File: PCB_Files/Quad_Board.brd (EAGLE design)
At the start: 81 x 76.2 mm, 39 parts

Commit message: Updates in layout
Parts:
- moved NAZE32_PINHEAD 6.35 mm to (54.6, 68.6)
- moved ULTRA1 6.35 mm to (12.7, 68.6)
- moved ULTRA4 6.35 mm to (30.5, 68.6)
- moved 5V_PDB 6.35 mm to (8.89, 26.7)
- moved BATTERY_MONITORING_PINS 6.35 mm to (73.7, 48.3)
- moved C1 6.35 mm to (58.4, 36.8)
- moved C10 6.35 mm to (30.5, 38.1)
- moved C15 6.35 mm to (57.1, 24.1)
- moved C2 6.35 mm to (52.1, 36.8)
- moved C3 6.35 mm to (29.2, 29.2)
- moved C4 6.35 mm to (24.1, 29.2)
- moved C7 6.35 mm to (22.9, 38.1)
- moved C9 6.35 mm to (35.6, 41.9)
- moved L1 6.35 mm to (40.6, 34.3)
- moved L2 6.35 mm to (50.8, 24.1)
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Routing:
- net P10.3: track 24.4 -> 48.1 mm, vias 2 -> 3
- net P9.3_5V: track 76.5 -> 74.5 mm, vias 2 -> 1
- net P9.3: track 66.6 -> 68.5 mm
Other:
- board text added: "rev 1.2"
- board text removed: "rev 1.0"

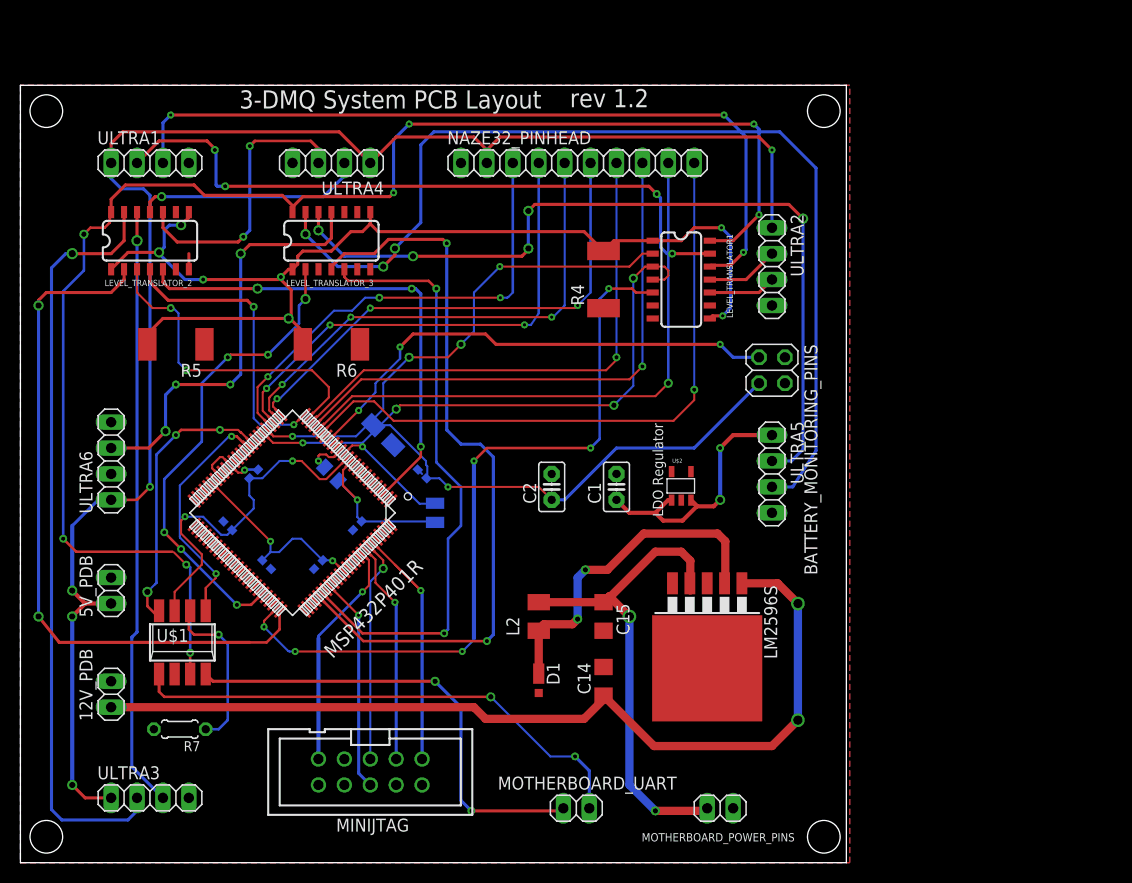
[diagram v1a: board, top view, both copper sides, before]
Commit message: Completed Schematic for PCB submission
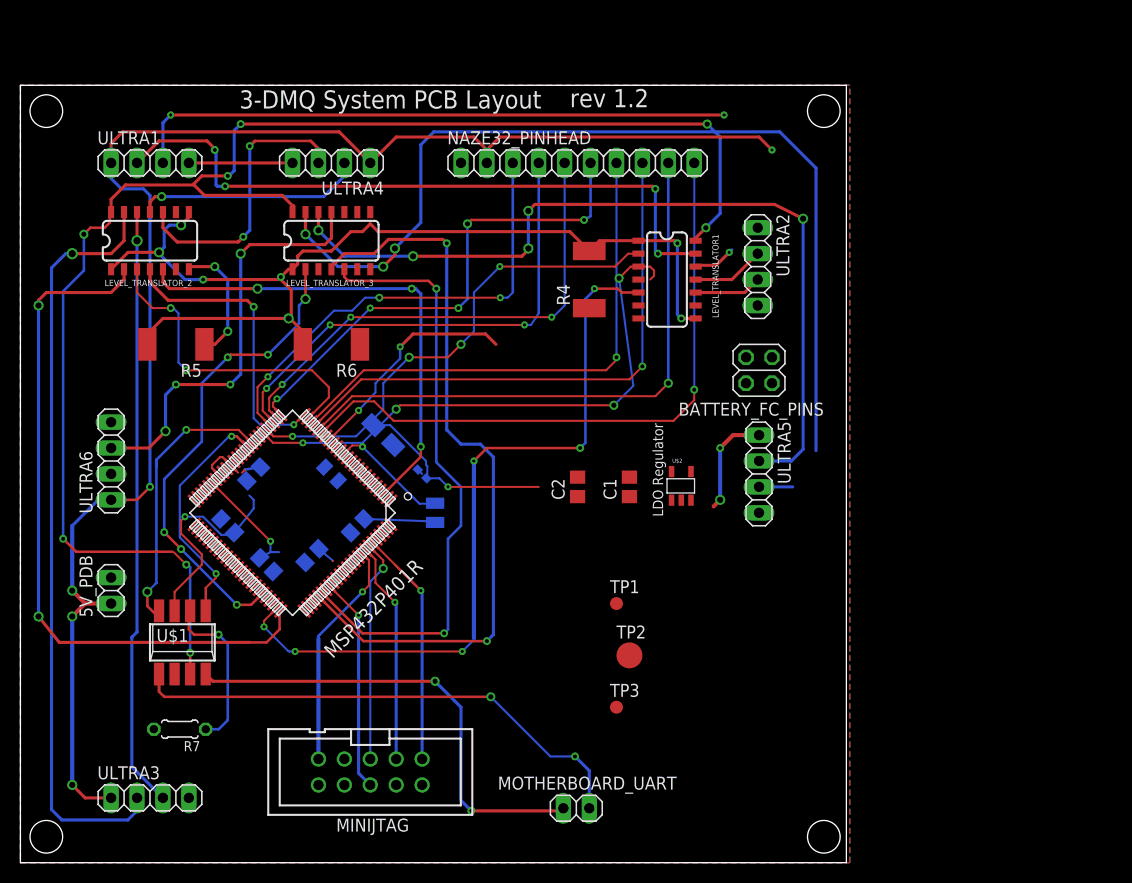
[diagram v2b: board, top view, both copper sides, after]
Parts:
- removed 12V_PDB, MOTHERBOARD_POWER_PINS: (no value), pinhead:1X02
- removed BATTERY_MONITORING_PINS: (no value), pinhead:2X02
- removed C14: 680u, eagle-ltspice:C1206
- removed C15: 220u, eagle-ltspice:C1206
- removed D1: PD3S160, diode:POWERDI323
- removed L2: 33u, resistor:L3225M
- removed LM2596S: LM2596S, national-semiconductor:TO263-5
- added BATTERY_FC_PINS: (no value), pinhead:2X02
- added TP1, TP3: TPB1,27, testpad:B1,27
- added TP2: TPB2,54, testpad:B2,54
- C1, C2: device capacitor-wima:C2.5-2 -> rcl:C0805
- C11, C3, C4, C7, C8: device rcl:0402 -> rcl:C0805
- R4, R5, R6: value (none) -> 100k
- moved C2 2.54 mm to (54.6, 36.8)
- moved LEVEL_TRANSLATOR1 1.40 mm to (63.4, 57.1)
- moved R4 1.40 mm to (55.8, 57.1)
- moved ULTRA2 1.40 mm to (72.3, 58.4)
- moved C1 1.27 mm to (59.7, 36.8)
- moved ULTRA5 1.27 mm to (72.4, 38.1)
- moved C3 1.09 mm to (28.6, 30.1)
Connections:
- removed net 12VDC: 12V_PDB.1, C14.1, LM2596S.1
- removed net MOTHEROARD_V+: C15.1, L2.2, LM2596S.4, MOTHERBOARD_POWER_PINS.1
- removed net N$4: D1.C, L2.1, LM2596S.2
- removed net OE: R7.1, U$1.6
- net 3V3: now also BATTERY_FC_PINS.3, R7.1, U$1.6; no longer BATTERY_MONITORING_PINS.3
- net GND: now also BATTERY_FC_PINS.2, BATTERY_FC_PINS.4, TP2.TP; no longer 12V_PDB.2, BATTERY_MONITORING_PINS.2, BATTERY_MONITORING_PINS.4, C14.2, C15.2, D1.A, LM2596S.3, LM2596S.5, MOTHERBOARD_POWER_PINS.2
- net P2.2_RX: now also BATTERY_FC_PINS.1, TP3.TP; no longer BATTERY_MONITORING_PINS.1
- net P7.7: now also TP1.TP
- net P8.1: no longer LEVEL_TRANSLATOR1.4
- net P8.2: now also LEVEL_TRANSLATOR1.4
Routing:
- net 12VDC: track 89.8 -> 0.00 mm, vias 2 -> 0
- net MOTHEROARD_V+: track 48.3 -> 0.00 mm, vias 2 -> 0
- net N$4: track 33.4 -> 0.00 mm, vias 2 -> 0
- net P2.2_RX: track 47.9 -> 21.6 mm, vias 3 -> 2
- net 3V3: track 81.5 -> 57.5 mm
- net 5VDC: track 183.4 -> 159.7 mm
- net GND: track 12.4 -> 29.3 mm
- net OE: track 16.3 -> 0.00 mm, vias 1 -> 0
- net P8.1_5V: track 77.6 -> 63.5 mm
- net VCORE: track 16.8 -> 6.99 mm, vias 1 -> 0
- net 3.3V: track 108.0 -> 100.4 mm
- net N$2: track 20.0 -> 13.7 mm, vias 2 -> 1
- net P5.6_5V: track 99.2 -> 96.3 mm
- net 5V: track 146.3 -> 148.0 mm
- net P8.0: track 49.4 -> 48.0 mm
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
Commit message: Updates in PCB Schematic and Layout
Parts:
- added GPIO_EXTRA: (no value), pinhead:1X05
- added R1: (no value), resistor:M1206
- added U$3: TXS0102, TXS0102-bi-directional-translator:SM8
- R4, R5, R6: device eagle-ltspice:R2512 -> resistor:M1206
- R7: device rcl:0204/5 -> resistor:M1206
- moved TP1 33.3 mm to (48.3, 57.1)
- moved MOTHERBOARD_UART 3.81 mm to (54.5, 9.14)
- moved ULTRA3 2.84 mm to (10.2, 7.62)
- moved C7 1.27 mm to (24.1, 38.1)
- moved MINIJTAG 1.27 mm to (34.3, 10.2)
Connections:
- removed net P4.0/A13: MSP432P401R.56
- removed net P4.1/A12: MSP432P401R.57
- removed net P4.5/A8: MSP432P401R.61
- removed net P4.6/A7: MSP432P401R.62
- removed net P4.7/A6: MSP432P401R.63
- new net P4.0_GPIO: GPIO_EXTRA.1, MSP432P401R.56
- new net P4.1_GPIO: GPIO_EXTRA.2, MSP432P401R.57
- new net P4.5_GPIO: GPIO_EXTRA.3, MSP432P401R.61
- new net P4.6_GPIO: GPIO_EXTRA.4, MSP432P401R.62
- new net P4.7_GPIO: GPIO_EXTRA.5, MSP432P401R.63
- new net VBAT_TX: BATTERY_FC_PINS.1, U$3.4
- net 3V3: now also R1.1, U$3.6, U$3.7
- net 5V: now also U$3.2
- net GND: now also R1.2, U$3.3
- net P2.2_RX: now also U$3.5; no longer BATTERY_FC_PINS.1
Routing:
- net P8.2: track 0.00 -> 65.2 mm, vias 0 -> 4
- net VBAT_TX: track 0.00 -> 46.8 mm, vias 0 -> 2
- net P6.7_5V: track 0.00 -> 44.5 mm, vias 0 -> 2
- net P5.6_5V: track 96.3 -> 67.3 mm, vias 3 -> 4
- net A2: track 46.1 -> 22.8 mm, vias 2 -> 1
- net P9.2: track 73.6 -> 51.6 mm, vias 6 -> 4
- net P2.2_RX: track 21.6 -> 0.00 mm, vias 2 -> 0
- net P9.3_5V: track 74.5 -> 64.1 mm
- net 3V3: track 57.5 -> 63.1 mm
- net P8.1: track 54.8 -> 49.4 mm
- net B2: track 50.8 -> 45.7 mm, vias 2 -> 1
- net 3.3V: track 100.4 -> 104.1 mm
- net GND: track 29.3 -> 32.9 mm, vias 2 -> 3
- net P10.4_5V: track 58.9 -> 56.1 mm
- net 5VDC: track 159.7 -> 162.2 mm
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
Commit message: Routing almost finalized
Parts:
- removed C10: 4u7, cap:CSMD0805
- removed C9: 10u, rcl:A/3216-18R
- added CPOLARISED: 10u, rcl:A/3216-18R
- added CPOLARIZED: 4u7, cap:CSMD0805
- R1: value (none) -> 100k
- moved TP3 23.7 mm to (56.8, 38.9)
- moved TP2 13.7 mm to (67.3, 8.89)
- moved R1 11.7 mm to (63.5, 29.2), turned to 270 degrees
- moved U$3 1.80 mm to (54.6, 27.9)
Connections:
- net 3V3: now also CPOLARISED.+; no longer C9.+
- net GND: now also CPOLARISED.-, CPOLARIZED.2; no longer C10.2, C9.-
- net VCORE: now also CPOLARIZED.1; no longer C10.1
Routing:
- net P4.0_GPIO: track 0.00 -> 89.2 mm, vias 0 -> 3
- net P5.7: track 0.00 -> 68.5 mm, vias 0 -> 6
- net P4.1_GPIO: track 0.00 -> 65.2 mm, vias 0 -> 2
- net P4.5_GPIO: track 0.00 -> 64.1 mm, vias 0 -> 2
- net P4.7_GPIO: track 0.00 -> 64.1 mm, vias 0 -> 1
- net P4.6_GPIO: track 0.00 -> 63.4 mm, vias 0 -> 1
- net 3V3: track 63.1 -> 121.1 mm, vias 3 -> 9
- net P2.2_RX: track 0.00 -> 43.3 mm, vias 0 -> 4
- net 5V: track 146.0 -> 188.2 mm, vias 10 -> 12
- net GND: track 32.9 -> 66.3 mm, vias 3 -> 8
- net 5VDC: track 162.2 -> 194.9 mm
- net P9.2: track 51.6 -> 73.4 mm, vias 4 -> 6
- net A2: track 22.8 -> 42.1 mm
- net P8.1_5V: track 62.8 -> 76.4 mm, vias 2 -> 4
- net VBAT_TX: track 46.8 -> 37.0 mm, vias 2 -> 1
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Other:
- board text added: "rev 2.2"
- board text removed: "rev 1.2"
